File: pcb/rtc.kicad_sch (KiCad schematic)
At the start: 2 parts, among them U3 SW_Push

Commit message: sus commit
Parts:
- removed AE1: Antenna, JLCImport:KH-GPS181804-WY, symbol Device:Antenna
- removed U3: SW_Push, symbol RF_GPS:MAX-M10S
- added C28: 100nF, Capacitor_SMD:C_0402_1005Metric, symbol Device:C_Small
- added U7: BQ24074RGT, Package_DFN_QFN:VQFN-16-1EP_3x3mm_P0.5mm_EP1.6x1.6mm, symbol Timer_RTC:RV-3028-C7
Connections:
- net +3V3: now also C28.1, U7.7 (VDD)
- net GND: now also C28.2, U7.5 (VSS), U7.8 (EVI)
- new net P0.23: U7.3 (SCL)
- new net P0.27: U7.4 (SDA)
- no-connect marks 6 -> 0

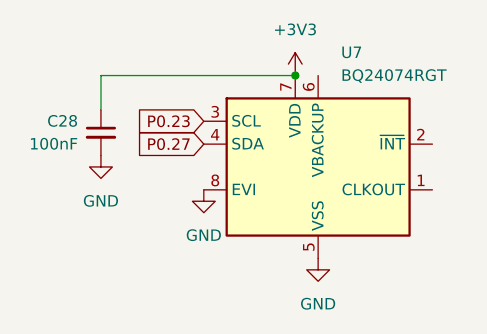
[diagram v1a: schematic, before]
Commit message: fix symbols getting absolutely goofed up
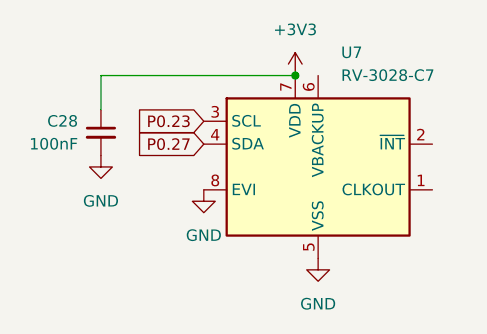
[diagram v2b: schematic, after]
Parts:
- U7: value BQ24074RGT -> RV-3028-C7; footprint Package_DFN_QFN:VQFN-16-1EP_3x3mm_P0.5mm_EP1.6x1.6mm -> Package_SON:MicroCrystal_C7_SON-8_1.5x3.2mm_P0.9mm
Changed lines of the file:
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@@
 			)
 		)
-		(property "Value" "BQ24074RGT"
+		(property "Value" "RV-3028-C7"
 			(at 147.32 86.36 0)
 			(show_name no)
@@
 			)
 		)
-		(property "Footprint" "Package_DFN_QFN:VQFN-16-1EP_3x3mm_P0.5mm_EP1.6x1.6mm"
+		(property "Footprint" "Package_SON:MicroCrystal_C7_SON-8_1.5x3.2mm_P0.9mm"
 			(at 170.18 105.41 0)
 			(hide yes)
@@
 			)
 		)
-		(property "Datasheet" "http://www.ti.com/lit/ds/symlink/bq24074.pdf"
+		(property "Datasheet" "https://www.microcrystal.com/fileadmin/Media/Products/RTC/Datasheet/RV-3028-C7.pdf"
 			(at 144.78 96.52 0)
 			(hide yes)
@@
 			)
 		)
-		(property "Description" "USB-Friendly Li-Ion Battery Charger and Power-Path Management, VQFN-16"
+		(property "Description" "Realtime Clock/Calendar I2C Interface, Extreme Low Power, 1.1 V to 5.5 V, MicroCrystal C7"
 			(at 144.78 96.52 0)
 			(hide yes)

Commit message: sussy
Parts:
- renumbered U7 to U8
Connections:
- net LF_EXT_CLK: now reaches U8.1 (CLKOUT)
- no-connect marks 0 -> 1
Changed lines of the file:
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@@
 		(color 0 0 0 0)
+	)
+	(no_connect
+		(at 157.48 93.98)
 	)
 	(wire
@@
 			(width 0)
 			(type default)
+		)
+	)
+	(global_label "LF_EXT_CLK"
+		(shape input)
+		(at 157.48 99.06 0)
+		(fields_autoplaced yes)
+		(effects
+			(font
+				(size 1.27 1.27)
+			)
+			(justify left)
+		)
+		(property "Intersheetrefs" "${INTERSHEET_REFS}"
+			(at 171.4113 99.06 0)
+			(hide yes)
+			(show_name no)
+			(do_not_autoplace no)
+			(effects
+				(font
+					(size 1.27 1.27)
+				)
+				(justify left)
+			)
 		)
 	)
@@
 		(dnp no)
 		(fields_autoplaced yes)
-		(property "Reference" "#PWR050"
+		(property "Reference" "#PWR054"
 			(at 120.65 101.6 0)
 			(hide yes)
@@
 			(project "watch"
 				(path "/55e581b0-f918-4a43-a276-2e38ad945bed"
-					(reference "#PWR050")
+					(reference "#PWR054")
 					(unit 1)
 				)
@@
 		(dnp no)
 		(fields_autoplaced yes)
-		(property "Reference" "#PWR049"
+		(property "Reference" "#PWR056"
 			(at 142.24 90.17 0)
 			(hide yes)
@@
 			(project "watch"
 				(path "/55e581b0-f918-4a43-a276-2e38ad945bed"
-					(reference "#PWR049")
+					(reference "#PWR056")
 					(unit 1)
 				)
@@
 		(in_pos_files yes)
 		(dnp no)
-		(property "Reference" "U7"
+		(property "Reference" "U8"
 			(at 147.32 83.82 0)
 			(show_name no)
@@
 			(project "watch"
 				(path "/55e581b0-f918-4a43-a276-2e38ad945bed"
-					(reference "U7")
+					(reference "U8")
 					(unit 1)
 				)
@@
 		(dnp no)
 		(fields_autoplaced yes)
-		(property "Reference" "#PWR051"
+		(property "Reference" "#PWR055"
 			(at 132.08 105.41 0)
 			(hide yes)
@@
 			(project "watch"
 				(path "/55e581b0-f918-4a43-a276-2e38ad945bed"
-					(reference "#PWR051")
+					(reference "#PWR055")
 					(unit 1)
 				)
@@
 		(dnp no)
 		(fields_autoplaced yes)
-		(property "Reference" "#PWR048"
+		(property "Reference" "#PWR057"
 			(at 144.78 113.03 0)
 			(hide yes)
@@
 			(project "watch"
 				(path "/55e581b0-f918-4a43-a276-2e38ad945bed"
-					(reference "#PWR048")
+					(reference "#PWR057")
 					(unit 1)
 				)

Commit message: amogus
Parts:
- added R15, R16: 10k, Resistor_SMD:R_0402_1005Metric, symbol Device:R
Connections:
- net +3V3: now also R15.1, R16.1
- net P0.23: now also R15.2
- net P0.27: now also R16.2
- no-connect marks 1 -> 2
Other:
- moved on the sheet: C28

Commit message: mogus
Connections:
- net P0.23 renamed P0.04
- net P0.27 renamed P0.26
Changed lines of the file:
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@@
 		)
 	)
-	(global_label "P0.27"
+	(global_label "P0.26"
 		(shape input)
 		(at 107.95 93.98 180)
@@
 		)
 	)
-	(global_label "P0.23"
+	(global_label "P0.04"
 		(shape input)
 		(at 107.95 91.44 180)
